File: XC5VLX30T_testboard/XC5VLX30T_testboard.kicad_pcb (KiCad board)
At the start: 4 copper layers, 19 parts, among them J1 Conn_01x35_Pin, J2 Conn_01x35_Pin, J3 Conn_01x35_Pin, J4 Conn_01x35_Pin, J5 Conn_01x35_Pin, J6 Conn_01x35_Pin, J7 Conn_01x35_Pin, J8 Conn_01x35_Pin, U1 XC5VLX30T-1FFG665C, X1 SG-5032CCN

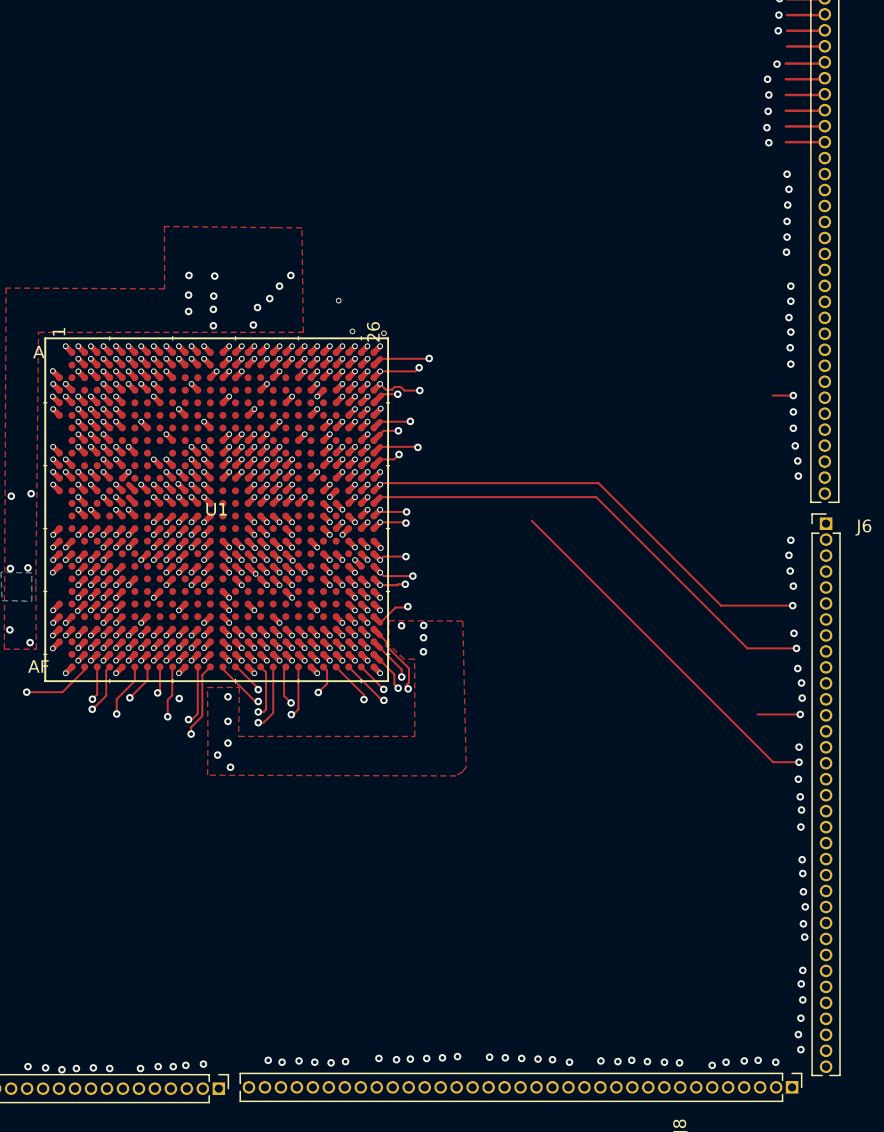
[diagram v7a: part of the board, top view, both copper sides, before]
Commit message: convert all vias to through hole
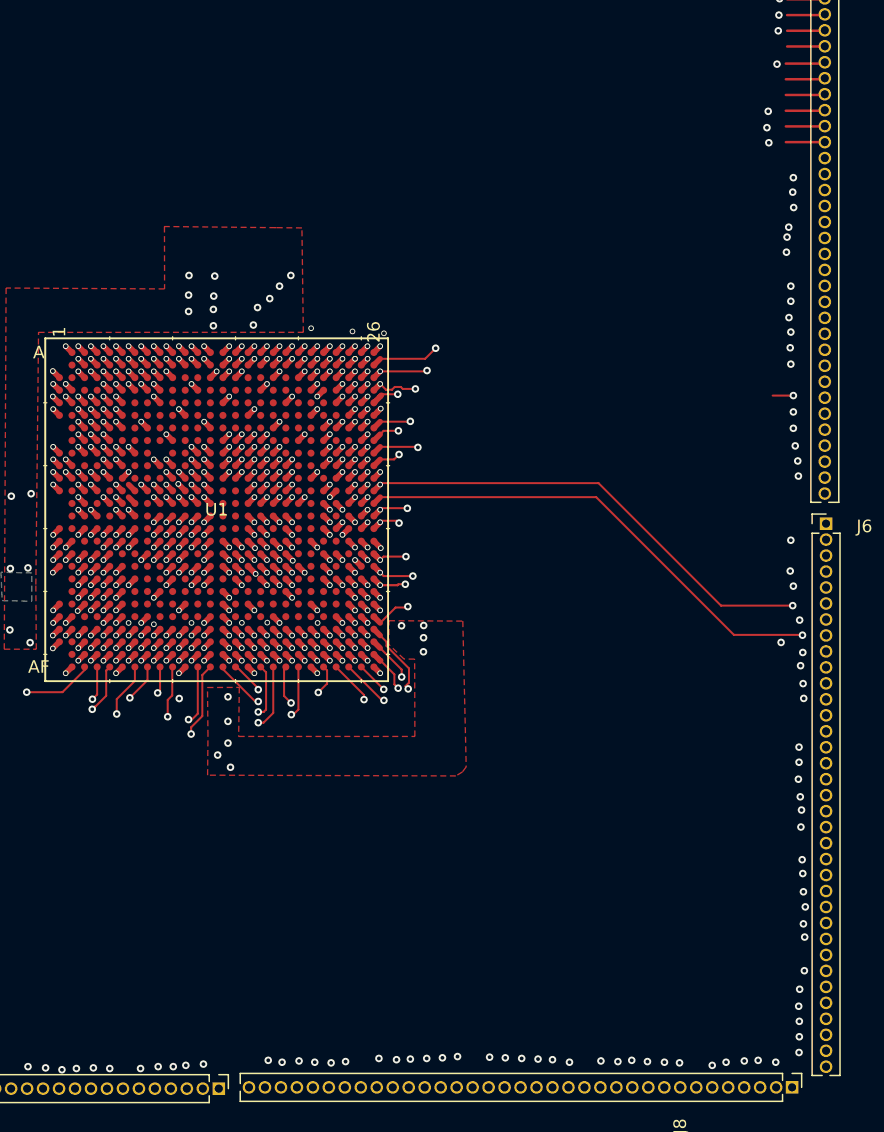
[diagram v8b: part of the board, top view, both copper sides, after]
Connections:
- J3 pad 21: GND -> unconnected-(J3-Pin_21-Pad21)
- J3 pad 22: unconnected-(J3-Pin_22-Pad22) -> GND
- J3 pad 23: unconnected-(J3-Pin_23-Pad23) -> GND
- J3 pad 24: unconnected-(J3-Pin_24-Pad24) -> VCCO
- J3 pad 25: unconnected-(J3-Pin_25-Pad25) -> VCCO
- J3 pad 26: unconnected-(J3-Pin_26-Pad26) -> VCCO
- J3 pad 27: unconnected-(J3-Pin_27-Pad27) -> VCCO
- J3 pad 29: unconnected-(J3-Pin_29-Pad29) -> GND
- J3 pad 30: unconnected-(J3-Pin_30-Pad30) -> vccext
- J3 pad 31: unconnected-(J3-Pin_31-Pad31) -> vccext
- J3 pad 32: unconnected-(J3-Pin_32-Pad32) -> vccext
- J3 pad 33: unconnected-(J3-Pin_33-Pad33) -> vccext
- J3 pad 34: unconnected-(J3-Pin_34-Pad34) -> vccext
- J3 pad 35: GND -> vccext
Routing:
- net IO_L18N_15: track 3.93 -> 42.4 mm, vias 3 -> 2
- net IO_L8P_CC_SM1P_13: track 20.8 -> 49.3 mm
- net IO_L0P_SM8P_13: track 18.8 -> 40.2 mm
- net IO_L6N_11: track 46.0 -> 66.0 mm
- net vccext: track 0.00 -> 17.2 mm
- net unconnected-(J3-Pin_30-Pad30): track 2.86 -> 0.00 mm
- net unconnected-(J3-Pin_34-Pad34): track 2.86 -> 0.00 mm
- net unconnected-(J3-Pin_32-Pad32): track 2.86 -> 0.00 mm
- net unconnected-(J3-Pin_31-Pad31): track 2.86 -> 0.00 mm
- net unconnected-(J3-Pin_33-Pad33): track 2.86 -> 0.00 mm
- net GND: track 121.1 -> 118.9 mm, vias 159 -> 160
- net IO_L19N_SM9N_11: track 40.0 -> 42.1 mm
- net IO_L11N_CC_13: track 55.2 -> 57.2 mm
- net IO_L12P_VRN_15: track 44.2 -> 42.5 mm, vias 2 -> 1
- net IO_L9P_CC_SM0P_13: track 51.3 -> 53.0 mm
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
